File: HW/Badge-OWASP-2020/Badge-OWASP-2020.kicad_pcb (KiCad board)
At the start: 2 copper layers, 98.6 x 65.9 mm, 33 parts, among them J1 Shitty Add-Ons, J2 Battery, J3 I2C, J4 USB_B, Q1 MMBT3904, Q2 DMG3415U-7, Q3 MMBT3904, SW1 RST, SW2 BOOT, U1 ESP32-WROOM-32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

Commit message: fix logos
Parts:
- moved R2 16.9 mm to (136.4, 69.1), turned to 0 degrees
- moved D3 13.4 mm to (151.8, 58.4)
- moved R1 12.6 mm to (151.4, 54.6)
- moved U2 12.2 mm to (155.1, 67.1)
- moved C1 11.6 mm to (151.4, 50.5)
- moved Q1 10.6 mm to (152.2, 83.1)
- moved G*** 5.11 mm to (145.5, 76.7)
- moved G*** 3.07 mm to (144.3, 72.1)
- moved R6 2.36 mm to (149.1, 87.4)
- moved G*** 2.05 mm to (134.9, 79.0)
- moved Q3 1.27 mm to (144.6, 85.9)
- moved R5 1.26 mm to (145.3, 81.8), turned to 180 degrees
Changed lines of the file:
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@@
-(kicad_pcb (version 20171130) (host pcbnew "(5.1.4-0-10_14)")
+(kicad_pcb (version 20171130) (host pcbnew "(5.1.4)-1")
   (general
     (thickness 1.6)
@@
     (35 F.Paste user)
     (36 B.SilkS user)
-    (37 F.SilkS user)
+    (37 F.SilkS user hide)
     (38 B.Mask user)
     (39 F.Mask user)
@@
   )
   (module Aesthetics:espressif (layer B.Cu)
-    (at 147.066 73.406 180)
+    (at 144.272 72.136 180)
     (fp_text reference G*** (at 0 0) (layer B.SilkS) hide
       (effects (font (size 1.524 1.524) (thickness 0.3)) (justify mirror))
@@
   )
   (module Aesthetics:pcbway_13x4 (layer B.Cu)
-    (at 145.034 81.788 180)
+    (at 145.542 76.708 180)
     (fp_text reference G*** (at 0 0) (layer B.SilkS) hide
       (effects (font (size 1.524 1.524) (thickness 0.3)) (justify mirror))
@@
   )
   (module Aesthetics:electronic_cats_logo_8x6 (layer B.Cu)
-    (at 135.89 77.216 180)
+    (at 134.874 78.994 180)
     (fp_text reference G*** (at 0 0) (layer B.SilkS) hide
       (effects (font (size 1.524 1.524) (thickness 0.3)) (justify mirror))
@@
   )
   (module Package_SO:SOIC-16_3.9x9.9mm_P1.27mm (layer B.Cu)
-    (at 158.75 78.74 90)
+    (at 155.067 67.121 90)
     (descr "SOIC, 16 Pin (JEDEC MS-012AC, https://www.analog.com/media/en/package-pcb-resources/package/pkg_pdf/soic_narrow-r/r_16.pdf), generated with kicad-footprint-generator ipc_gullwing_generator.py")
     (tags "SOIC SO")
@@
   )
   (module Resistor_SMD:R_0805_2012Metric_Pad1.15x1.40mm_HandSolder (layer B.Cu)
-    (at 149.606 85.081 90)
+    (at 149.098 87.385 90)
     (descr "Resistor SMD 0805 (2012 Metric), square (rectangular) end terminal, IPC_7351 nominal with elongated pad for handsoldering. (Body size source: https://docs.google.com/spreadsheets/d/1BsfQQcO9C6DZCsRaXUlFlo91Tg2WpOkGARC1WS5S8t0/edit?usp=sharing), generated with kicad-footprint-generator")
     (tags "resistor handsolder")
@@
   )
   (module Resistor_SMD:R_0805_2012Metric_Pad1.15x1.40mm_HandSolder (layer B.Cu)
-    (at 144.526 80.772)
+    (at 145.279 81.788 180)
     (descr "Resistor SMD 0805 (2012 Metric), square (rectangular) end terminal, IPC_7351 nominal with elongated pad for handsoldering. (Body size source: https://docs.google.com/spreadsheets/d/1BsfQQcO9C6DZCsRaXUlFlo91Tg2WpOkGARC1WS5S8t0/edit?usp=sharing), generated with kicad-footprint-generator")
     (tags "resistor handsolder")
@@
     (fp_line (start -1 0.6) (end 1 0.6) (layer B.Fab) (width 0.1))
     (fp_line (start -1 -0.6) (end -1 0.6) (layer B.Fab) (width 0.1))
-    (pad 2 smd roundrect (at 1.025 0) (size 1.15 1.4) (layers B.Cu B.Paste B.Mask) (roundrect_rratio 0.217391)
+    (pad 2 smd roundrect (at 1.025 0 180) (size 1.15 1.4) (layers B.Cu B.Paste B.Mask) (roundrect_rratio 0.217391)
       (net 17 /DTR))
-    (pad 1 smd roundrect (at -1.025 0) (size 1.15 1.4) (layers B.Cu B.Paste B.Mask) (roundrect_rratio 0.217391)
+    (pad 1 smd roundrect (at -1.025 0 180) (size 1.15 1.4) (layers B.Cu B.Paste B.Mask) (roundrect_rratio 0.217391)
       (net 16 "Net-(Q1-Pad1)"))
     (model ${KISYS3DMOD}/Resistor_SMD.3dshapes/R_0805_2012Metric.wrl
@@
   )
   (module Resistor_SMD:R_0805_2012Metric_Pad1.15x1.40mm_HandSolder (layer B.Cu)
-    (at 149.86 79.248 90)
+    (at 136.389 69.088)
     (descr "Resistor SMD 0805 (2012 Metric), square (rectangular) end terminal, IPC_7351 nominal with elongated pad for handsoldering. (Body size source: https://docs.google.com/spreadsheets/d/1BsfQQcO9C6DZCsRaXUlFlo91Tg2WpOkGARC1WS5S8t0/edit?usp=sharing), generated with kicad-footprint-generator")
     (tags "resistor handsolder")
     (attr smd)
-    (fp_text reference R2 (at 0 1.65 90) (layer B.SilkS)
+    (fp_text reference R2 (at 0 1.65) (layer B.SilkS)
       (effects (font (size 1 1) (thickness 0.15)) (justify mirror))
     )
-    (fp_text value 470 (at 0 -1.65 90) (layer B.Fab)
+    (fp_text value 470 (at 0 -1.65) (layer B.Fab)
       (effects (font (size 1 1) (thickness 0.15)) (justify mirror))
     )
-    (fp_text user %R (at 0 0 90) (layer B.Fab)
+    (fp_text user %R (at 0 0) (layer B.Fab)
       (effects (font (size 0.5 0.5) (thickness 0.08)) (justify mirror))
     )
@@
     (fp_line (start -1 0.6) (end 1 0.6) (layer B.Fab) (width 0.1))
     (fp_line (start -1 -0.6) (end -1 0.6) (layer B.Fab) (width 0.1))
-    (pad 2 smd roundrect (at 1.025 0 90) (size 1.15 1.4) (layers B.Cu B.Paste B.Mask) (roundrect_rratio 0.217391)
+    (pad 2 smd roundrect (at 1.025 0) (size 1.15 1.4) (layers B.Cu B.Paste B.Mask) (roundrect_rratio 0.217391)
       (net 19 "Net-(R2-Pad2)"))
-    (pad 1 smd roundrect (at -1.025 0 90) (size 1.15 1.4) (layers B.Cu B.Paste B.Mask) (roundrect_rratio 0.217391)
+    (pad 1 smd roundrect (at -1.025 0) (size 1.15 1.4) (layers B.Cu B.Paste B.Mask) (roundrect_rratio 0.217391)
       (net 5 /NP))
     (model ${KISYS3DMOD}/Resistor_SMD.3dshapes/R_0805_2012Metric.wrl
@@
   )
   (module Resistor_SMD:R_0805_2012Metric_Pad1.15x1.40mm_HandSolder (layer B.Cu)
-    (at 157.734 65.532)
+    (at 151.393 54.61)
     (descr "Resistor SMD 0805 (2012 Metric), square (rectangular) end terminal, IPC_7351 nominal with elongated pad for handsoldering. (Body size source: https://docs.google.com/spreadsheets/d/1BsfQQcO9C6DZCsRaXUlFlo91Tg2WpOkGARC1WS5S8t0/edit?usp=sharing), generated with kicad-footprint-generator")
     (tags "resistor handsolder")
@@
   )
   (module Package_TO_SOT_SMD:SOT-23 (layer B.Cu)
-    (at 143.576 85.106 90)
+    (at 144.592 85.868 90)
     (descr "SOT-23, Standard")
     (tags SOT-23)
@@
   )
   (module Package_TO_SOT_SMD:SOT-23 (layer B.Cu)
-    (at 144.338 75.962 90)
+    (at 152.212 83.074 90)
     (descr "SOT-23, Standard")
     (tags SOT-23)
@@
   )
   (module Diode_SMD:D_SOD-123F (layer B.Cu)
-    (at 157.864 70.358 180)
+    (at 151.768 58.42 180)
     (descr D_SOD-123F)
     (tags D_SOD-123F)
@@
   )
   (module Capacitor_SMD:C_0805_2012Metric_Pad1.15x1.40mm_HandSolder (layer B.Cu)
-    (at 157.471 60.452)
+    (at 151.393 50.546)
     (descr "Capacitor SMD 0805 (2012 Metric), square (rectangular) end terminal, IPC_7351 nominal with elongated pad for handsoldering. (Body size source: https://docs.google.com/spreadsheets/d/1BsfQQcO9C6DZCsRaXUlFlo91Tg2WpOkGARC1WS5S8t0/edit?usp=sharing), generated with kicad-footprint-generator")
     (tags "capacitor handsolder")

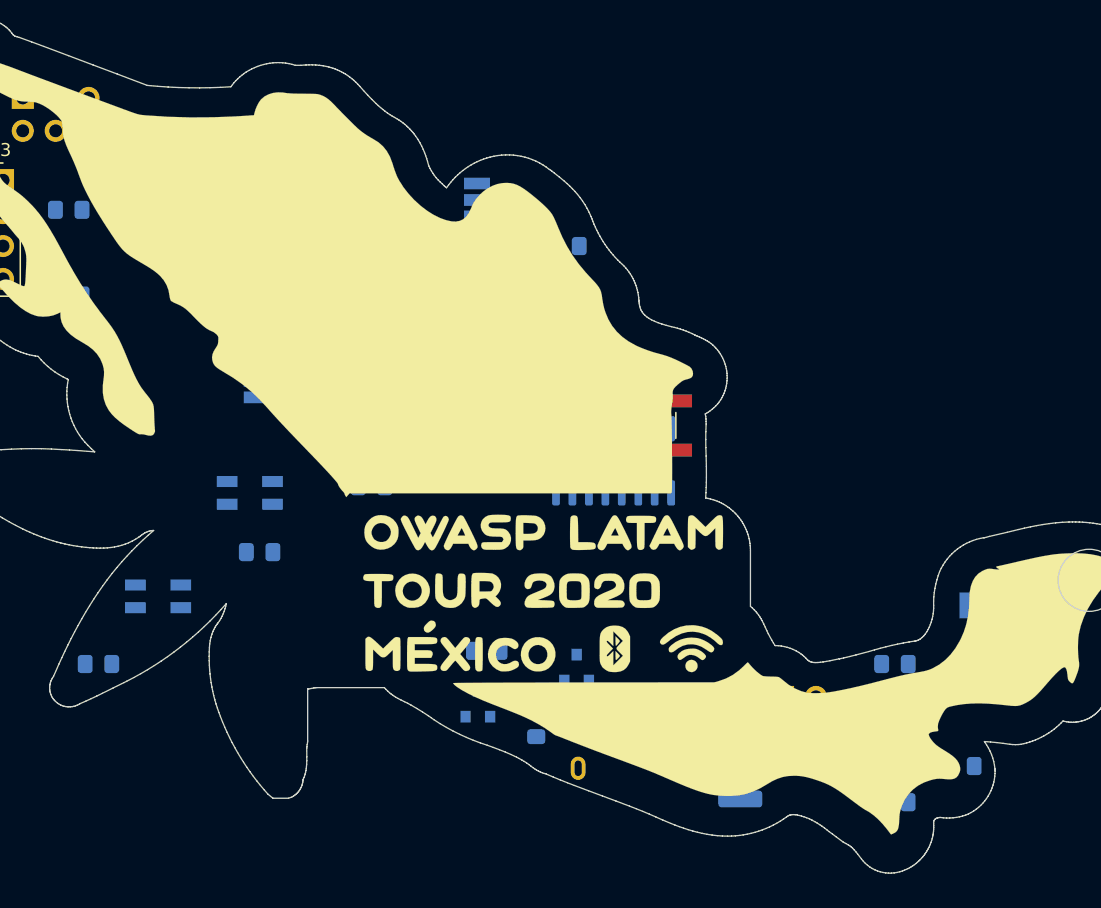
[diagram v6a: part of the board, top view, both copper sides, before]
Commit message: Add USB connector from LCSC change angle of components
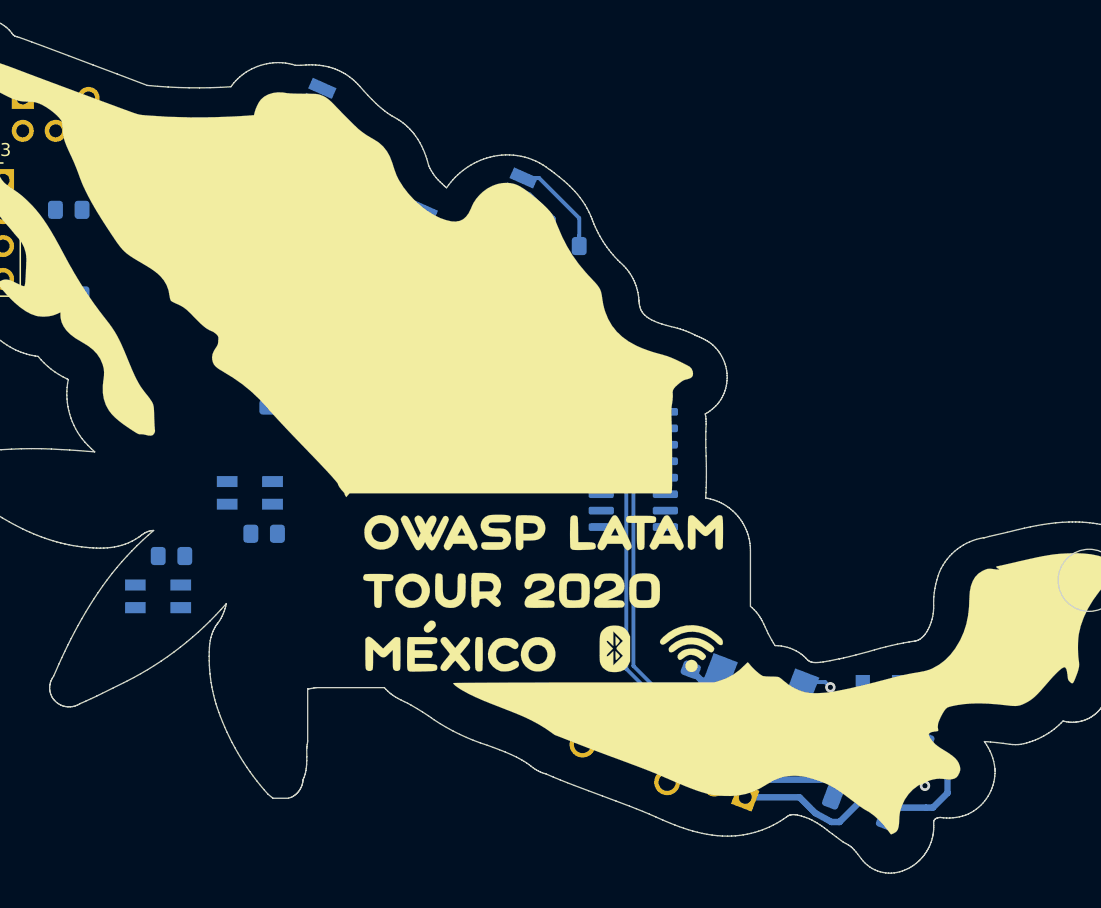
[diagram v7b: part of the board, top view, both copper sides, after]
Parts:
- J4: value USB_B -> USB_B_Micro; footprint Connector_USB:USB_Micro-B_Wuerth_629105150521 -> Connectors:U254051N4BH806
- moved D3 35.2 mm to (175.7, 84.2), turned to 0 degrees
- moved SW2 27.8 mm to (123.7, 48.8), turned to 156 degrees
- moved R6 22.4 mm to (145.2, 65.3), turned to 0 degrees
- moved C4 22.2 mm to (160.7, 84.2), turned to 249 degrees
- moved U3 18.1 mm to (166.0, 85.2), turned to 159 degrees
- moved Q3 17.9 mm to (145.4, 68.0), turned to 180 degrees
- moved Q1 17.3 mm to (148.8, 66.1), turned to 0 degrees
- moved R5 13.5 mm to (148.9, 68.8), turned to 0 degrees
- moved SW1 12.4 mm to (146.1, 58.7), turned to 156 degrees
- moved R2 10.7 mm to (128.4, 62.0), turned to 90 degrees
- moved C3 10.1 mm to (121.0, 74.5)
- moved F1 9.75 mm to (174.4, 93.1), turned to 159 degrees
- moved G*** 9.53 mm to (147.2, 81.2), turned to 156 degrees
- moved J2 8.28 mm to (165.2, 93.1), turned to 69 degrees
- moved C5 8.26 mm to (170.8, 88.5), turned to 69 degrees
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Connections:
- J4 pad 4: GND -> Net-(J4-Pad4)
- J4 pad 6: (no net) -> GND
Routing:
- net /D-: track 0.00 -> 24.8 mm
- net Net-(F1-Pad2): track 0.00 -> 23.9 mm
- net /D+: track 0.00 -> 23.1 mm
- net GND: track 0.00 -> 17.0 mm, vias 0 -> 4
- net Net-(C5-Pad1): track 0.00 -> 16.5 mm
- net +3V3: track 0.00 -> 16.4 mm
- net /EN: track 0.00 -> 16.1 mm
- net +BATT: track 0.00 -> 15.8 mm
- net VCC: track 0.00 -> 15.7 mm
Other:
- net class Default: clearance 0.2 -> 0.25; trace_width 0.25 -> 0.3
- net class vcc added: clearance 0.3, trace_width 0.5, via_dia 0.8, via_drill 0.4
- rule trace_clearance: 0.2 -> 0.25

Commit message: routeo
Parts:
- moved J3 9.16 mm to (108.5, 54.6), turned to 180 degrees
- moved R3 7.37 mm to (112.8, 47.0), turned to 0 degrees
- moved C3 3.53 mm to (123.4, 77.0), turned to 90 degrees
- moved R4 1.79 mm to (112.8, 49.5), turned to 0 degrees
- moved SW1 1.13 mm to (146.5, 57.6)
- moved D2 0.18 mm to (119.8, 77.7), turned to 90 degrees
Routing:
- net +3V3: track 16.4 -> 150.1 mm, vias 0 -> 4
- net /SDA: track 0.00 -> 47.2 mm, vias 0 -> 1
- net /GPIO1: track 0.00 -> 46.8 mm, vias 0 -> 1
- net /RX: track 0.00 -> 44.4 mm, vias 0 -> 2
- net /TX: track 0.00 -> 44.2 mm, vias 0 -> 2
- net GND: track 17.0 -> 57.4 mm
- net /GPIO0: track 0.00 -> 38.1 mm, vias 0 -> 1
- net /SCL: track 0.00 -> 37.4 mm, vias 0 -> 1
- net /DTR: track 0.00 -> 30.5 mm, vias 0 -> 2
- net /RTS: track 0.00 -> 22.3 mm
- net /GPIO2: track 0.00 -> 20.3 mm
- net /EN: track 16.1 -> 30.5 mm, vias 0 -> 2
- net Net-(D1-Pad2): track 0.00 -> 10.9 mm
- net /NP: track 0.00 -> 9.94 mm
- net Net-(Q3-Pad1): track 0.00 -> 3.61 mm
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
